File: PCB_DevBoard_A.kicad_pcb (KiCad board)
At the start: 2 copper layers, 83 x 71 mm, 55 parts, among them J1 Conn_01x05, J2 Conn_01x05, J3 Debug, J5 I/O A, J6 I/O B, U1 TLV1117-33, U2 XMC1404_F064, U3 TLE7251, U4 ULN2003A, U5 ULN2003A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

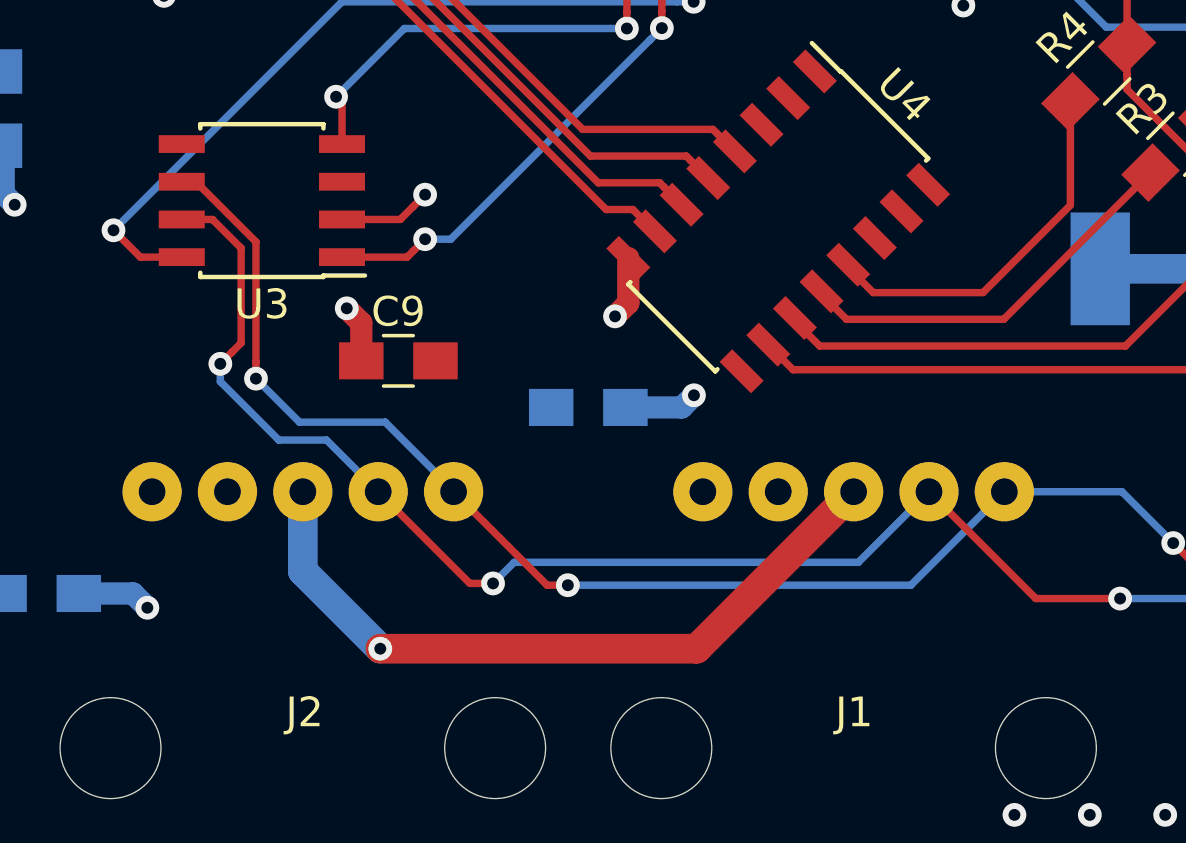
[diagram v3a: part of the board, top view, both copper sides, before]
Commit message: Improve the tracks between the connectors
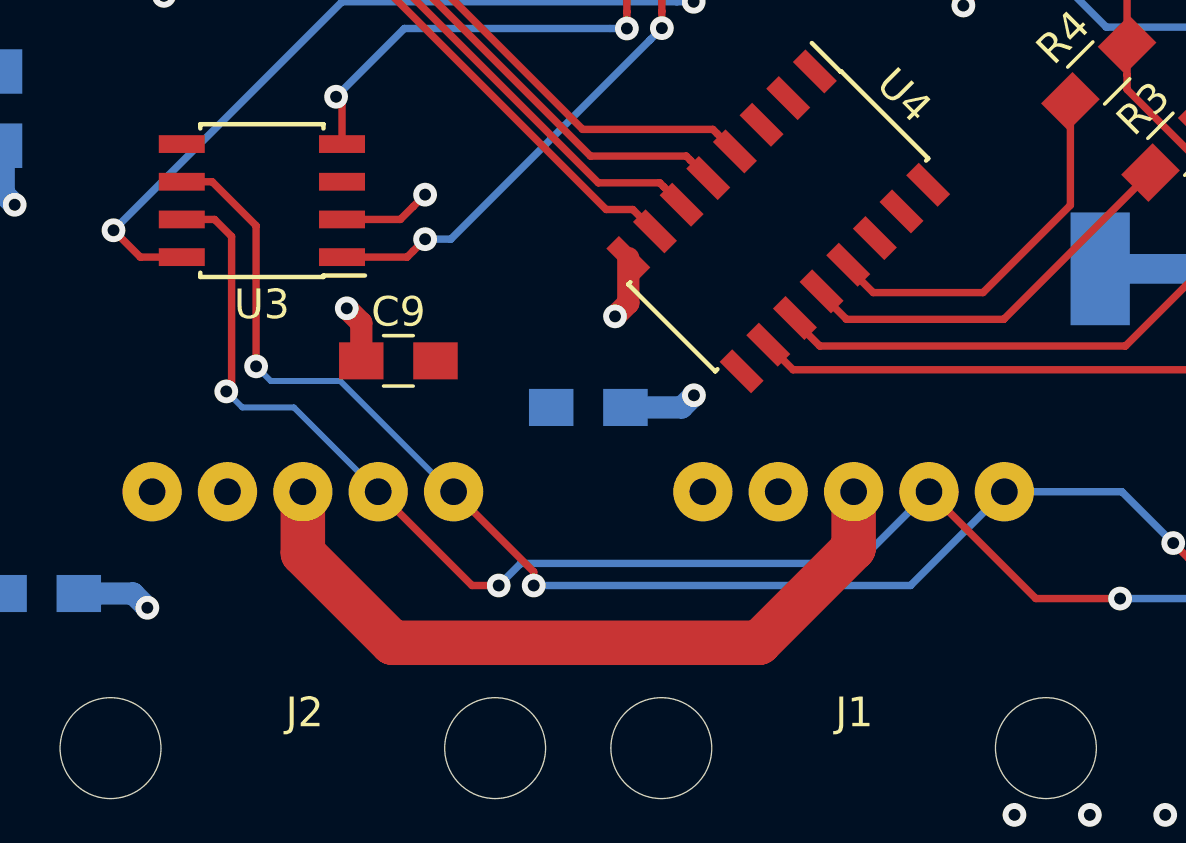
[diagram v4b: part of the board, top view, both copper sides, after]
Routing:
- net +BATT: track 24.5 -> 25.1 mm, vias 1 -> 0
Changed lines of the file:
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@@
     (thickness 1.6)
     (drawings 21)
-    (tracks 711)
+    (tracks 709)
     (zones 0)
     (modules 55)
@@
   )
   (setup
-    (last_trace_width 0.75)
+    (last_trace_width 1.5)
     (user_trace_width 0.75)
     (user_trace_width 1)
+    (user_trace_width 1.5)
     (trace_clearance 0.2)
     (zone_clearance 0.45)
@@
     (via_min_size 0.4)
     (via_min_drill 0.3)
+    (user_via 1.5 0.75)
     (uvia_size 0.3)
     (uvia_drill 0.1)
@@
   (segment (start 121.5 132.15) (end 121.25 132.15) (width 0.25) (layer F.Cu) (net 5))
   (segment (start 121.25 132.15) (end 118.825 134.575) (width 0.25) (layer F.Cu) (net 5))
-  (segment (start 125.3 150.465) (end 125.775 150.465) (width 0.25) (layer F.Cu) (net 6))
-  (segment (start 125.775 150.465) (end 127.80001 152.49001) (width 0.25) (layer F.Cu) (net 6))
-  (segment (start 127.80001 152.49001) (end 127.80001 156.534324) (width 0.25) (layer F.Cu) (net 6))
-  (segment (start 127.80001 156.534324) (end 127.80001 157.100009) (width 0.25) (layer F.Cu) (net 6))
-  (via (at 127.80001 157.100009) (size 0.8) (drill 0.4) (layers F.Cu B.Cu) (net 6))
-  (via (at 138.31 164.06) (size 0.8) (drill 0.4) (layers F.Cu B.Cu) (net 6))
-  (segment (start 134.46 160.91) (end 137.61 164.06) (width 0.25) (layer F.Cu) (net 6))
-  (segment (start 137.61 164.06) (end 138.31 164.06) (width 0.25) (layer F.Cu) (net 6))
-  (segment (start 153.02 160.91) (end 149.87 164.06) (width 0.25) (layer B.Cu) (net 6))
-  (segment (start 149.87 164.06) (end 138.31 164.06) (width 0.25) (layer B.Cu) (net 6))
   (via (at 158.71 162.64) (size 0.8) (drill 0.4) (layers F.Cu B.Cu) (net 6))
   (segment (start 165.37 163.17) (end 159.24 163.17) (width 0.25) (layer F.Cu) (net 6))
@@
   (segment (start 156.98 160.91) (end 158.71 162.64) (width 0.25) (layer B.Cu) (net 6))
   (segment (start 134.46 160.91) (end 134.46 160.87) (width 0.25) (layer B.Cu) (net 6))
-  (segment (start 134.46 160.87) (end 132.154999 158.564999) (width 0.25) (layer B.Cu) (net 6))
-  (segment (start 132.154999 158.564999) (end 129.265001 158.564999) (width 0.25) (layer B.Cu) (net 6))
-  (segment (start 129.265001 158.564999) (end 127.80001 157.100009) (width 0.25) (layer B.Cu) (net 6))
-  (via (at 126.6 156.6) (size 0.8) (drill 0.4) (layers F.Cu B.Cu) (net 7))
-  (segment (start 126.999999 156.200001) (end 126.6 156.6) (width 0.25) (layer F.Cu) (net 7))
-  (segment (start 127.3 155.9) (end 126.999999 156.200001) (width 0.25) (layer F.Cu) (net 7))
-  (segment (start 127.3 152.7) (end 127.3 155.9) (width 0.25) (layer F.Cu) (net 7))
-  (segment (start 125.3 151.735) (end 126.335 151.735) (width 0.25) (layer F.Cu) (net 7))
-  (segment (start 126.335 151.735) (end 127.3 152.7) (width 0.25) (layer F.Cu) (net 7))
-  (via (at 135.79 164.000002) (size 0.8) (drill 0.4) (layers F.Cu B.Cu) (net 7))
-  (segment (start 131.92 160.91) (end 135.010002 164.000002) (width 0.25) (layer F.Cu) (net 7))
-  (segment (start 135.010002 164.000002) (end 135.79 164.000002) (width 0.25) (layer F.Cu) (net 7))
-  (segment (start 150.48 160.91) (end 148.099983 163.290017) (width 0.25) (layer B.Cu) (net 7))
-  (segment (start 148.099983 163.290017) (end 136.499985 163.290017) (width 0.25) (layer B.Cu) (net 7))
-  (segment (start 136.499985 163.290017) (end 135.79 164.000002) (width 0.25) (layer B.Cu) (net 7))
+  (via (at 127.804992 156.685008) (size 0.8) (drill 0.4) (layers F.Cu B.Cu) (net 6))
+  (segment (start 125.3 150.465) (end 126.325 150.465) (width 0.25) (layer F.Cu) (net 6))
+  (segment (start 126.325 150.465) (end 127.804992 151.944992) (width 0.25) (layer F.Cu) (net 6))
+  (segment (start 127.804992 151.944992) (end 127.804992 156.685008) (width 0.25) (layer F.Cu) (net 6))
+  (segment (start 128.299984 157.18) (end 127.804992 156.685008) (width 0.2) (layer B.Cu) (net 6))
+  (segment (start 130.64 157.18) (end 128.299984 157.18) (width 0.2) (layer B.Cu) (net 6))
+  (segment (start 134.37 160.91) (end 130.64 157.18) (width 0.2) (layer B.Cu) (net 6))
+  (segment (start 134.46 160.91) (end 134.37 160.91) (width 0.2) (layer B.Cu) (net 6))
+  (segment (start 153.02 160.91) (end 149.859998 164.070002) (width 0.25) (layer B.Cu) (net 6))
+  (via (at 137.16 164.070002) (size 0.8) (drill 0.4) (layers F.Cu B.Cu) (net 6))
+  (segment (start 149.859998 164.070002) (end 137.16 164.070002) (width 0.25) (layer B.Cu) (net 6))
+  (segment (start 134.46 160.91) (end 137.16 163.61) (width 0.25) (layer F.Cu) (net 6))
+  (segment (start 137.16 163.61) (end 137.16 164.070002) (width 0.25) (layer F.Cu) (net 6))
   (via (at 156.92 164.51) (size 0.8) (drill 0.4) (layers F.Cu B.Cu) (net 7))
   (segment (start 150.48 160.91) (end 154.08 164.51) (width 0.25) (layer F.Cu) (net 7))
@@
   (segment (start 165.56 167.47) (end 162.6 164.51) (width 0.25) (layer B.Cu) (net 7))
   (segment (start 162.6 164.51) (end 156.92 164.51) (width 0.25) (layer B.Cu) (net 7))
-  (segment (start 126.6 156.6) (end 126.6 157.2) (width 0.25) (layer B.Cu) (net 7))
-  (segment (start 126.6 157.2) (end 128.57 159.17) (width 0.25) (layer B.Cu) (net 7))
-  (segment (start 128.57 159.17) (end 130.18 159.17) (width 0.25) (layer B.Cu) (net 7))
-  (segment (start 130.18 159.17) (end 131.92 160.91) (width 0.25) (layer B.Cu) (net 7))
+  (via (at 126.8 157.53) (size 0.8) (drill 0.4) (layers F.Cu B.Cu) (net 7))
+  (segment (start 127.34 158.07) (end 126.8 157.53) (width 0.2) (layer B.Cu) (net 7))
+  (segment (start 129.08 158.07) (end 127.34 158.07) (width 0.2) (layer B.Cu) (net 7))
+  (segment (start 131.92 160.91) (end 129.08 158.07) (width 0.2) (layer B.Cu) (net 7))
+  (segment (start 126.98 157.35) (end 126.8 157.53) (width 0.25) (layer F.Cu) (net 7))
+  (segment (start 126.98 152.31) (end 126.98 157.35) (width 0.25) (layer F.Cu) (net 7))
+  (segment (start 126.405 151.735) (end 126.98 152.31) (width 0.25) (layer F.Cu) (net 7))
+  (segment (start 125.3 151.735) (end 126.405 151.735) (width 0.25) (layer F.Cu) (net 7))
+  (via (at 135.980002 164.07) (size 0.8) (drill 0.4) (layers F.Cu B.Cu) (net 7))
+  (segment (start 131.92 160.91) (end 135.08 164.07) (width 0.25) (layer F.Cu) (net 7))
+  (segment (start 135.08 164.07) (end 135.980002 164.07) (width 0.25) (layer F.Cu) (net 7))
+  (segment (start 136.725004 163.324998) (end 135.980002 164.07) (width 0.25) (layer B.Cu) (net 7))
+  (segment (start 148.065002 163.324998) (end 136.725004 163.324998) (width 0.25) (layer B.Cu) (net 7))
+  (segment (start 150.48 160.91) (end 148.065002 163.324998) (width 0.25) (layer B.Cu) (net 7))
   (segment (start 126.41 109.875) (end 126.41 111.95) (width 0.25) (layer F.Cu) (net 8))
   (segment (start 133.7 119.24) (end 133.7 120.134315) (width 0.25) (layer F.Cu) (net 8))
@@
   (segment (start 129.749967 138.989373) (end 130.484568 138.254772) (width 0.25) (layer F.Cu) (net 80))
   (segment (start 140.5 151.4) (end 139.6 151.4) (width 0.25) (layer F.Cu) (net 80))
-  (via (at 131.99 166.2) (size 0.8) (drill 0.4) (layers F.Cu B.Cu) (net 104))
-  (segment (start 142.65 166.2) (end 131.99 166.2) (width 1) (layer F.Cu) (net 104))
-  (segment (start 147.94 160.91) (end 142.65 166.2) (width 1) (layer F.Cu) (net 104))
-  (segment (start 129.38 163.59) (end 131.99 166.2) (width 1) (layer B.Cu) (net 104))
-  (segment (start 129.38 160.91) (end 129.38 163.59) (width 1) (layer B.Cu) (net 104))
+  (segment (start 147.94 162.81) (end 147.94 160.91) (width 1.5) (layer F.Cu) (net 104))
+  (segment (start 132.4 166) (end 144.75 166) (width 1.5) (layer F.Cu) (net 104))
+  (segment (start 129.38 162.98) (end 132.4 166) (width 1.5) (layer F.Cu) (net 104))
+  (segment (start 144.75 166) (end 147.94 162.81) (width 1.5) (layer F.Cu) (net 104))
+  (segment (start 129.38 160.91) (end 129.38 162.98) (width 1.5) (layer F.Cu) (net 104))
   (segment (start 168.07 167.44) (end 168.1 167.47) (width 0.25) (layer F.Cu) (net 105))
   (segment (start 168.07 163.17) (end 168.07 167.44) (width 0.25) (layer F.Cu) (net 105))

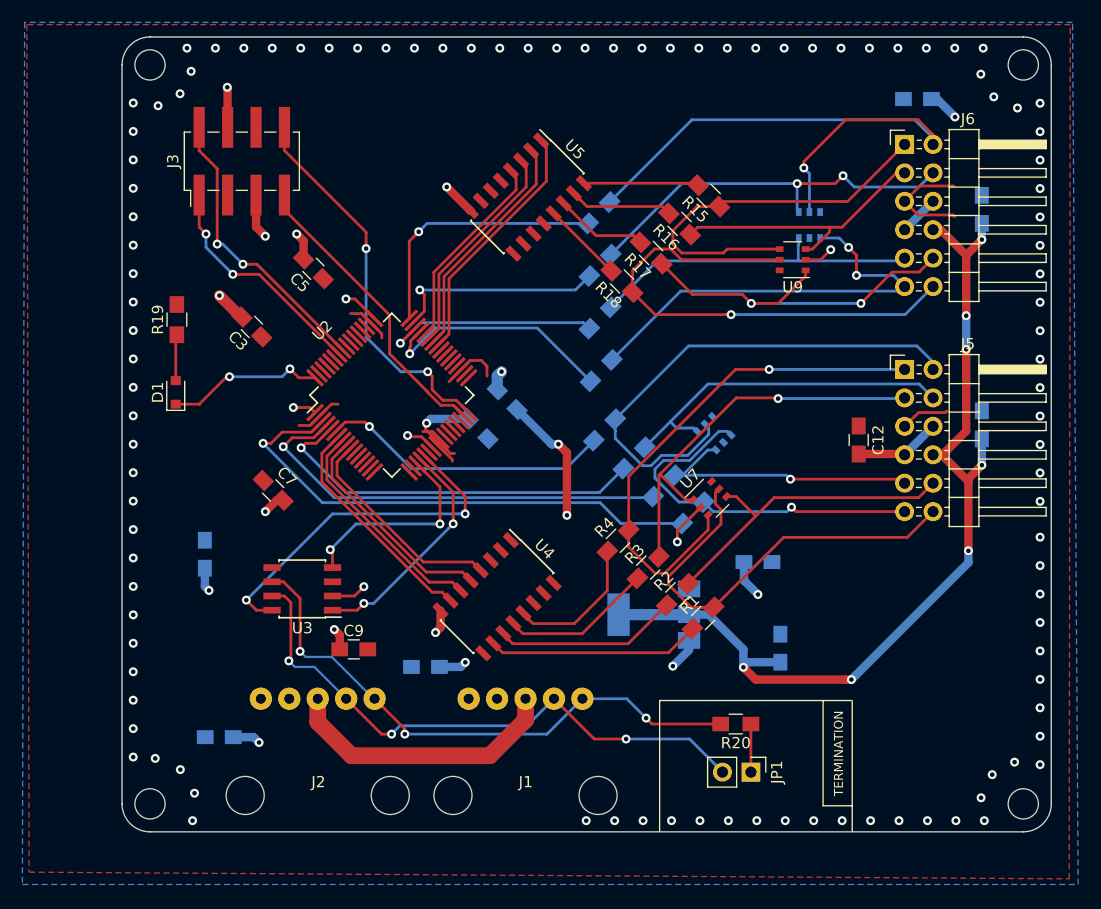
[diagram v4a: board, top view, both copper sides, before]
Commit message: Remove the ground vias around the edges
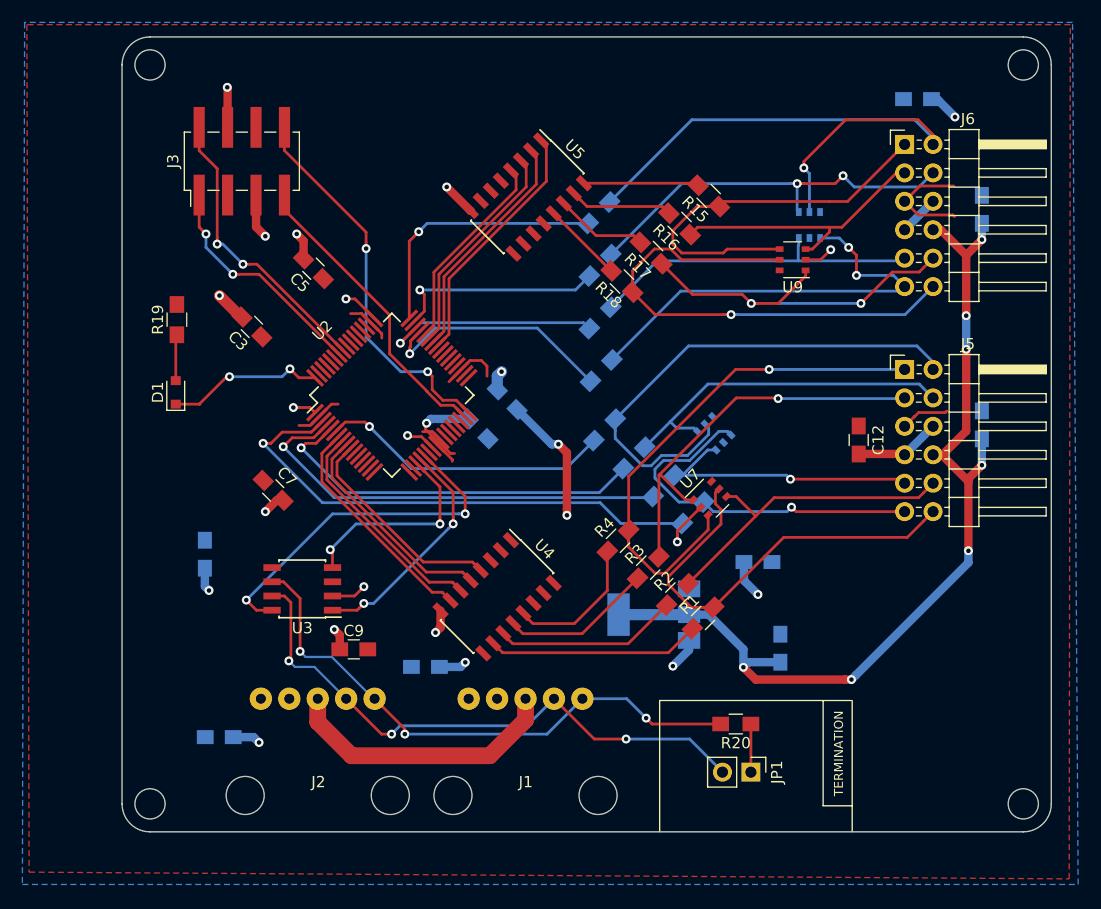
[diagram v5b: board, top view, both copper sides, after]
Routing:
- net GND: vias 121 -> 16

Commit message: Update logotypes etc.
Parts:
- removed the G*** at (129.9, 112.0)
- added G***: LOGO, DevBoard:Text_Wolley_DevECU_14mm_SilkScreen, B.Cu at (121.2, 126.5)
- G***: moved to F.Cu
- moved G*** 60.8 mm to (184.2, 157.2), turned to 0 degrees
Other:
- board text added: "BUS"
- board text removed: "DevBoard A 1.0"

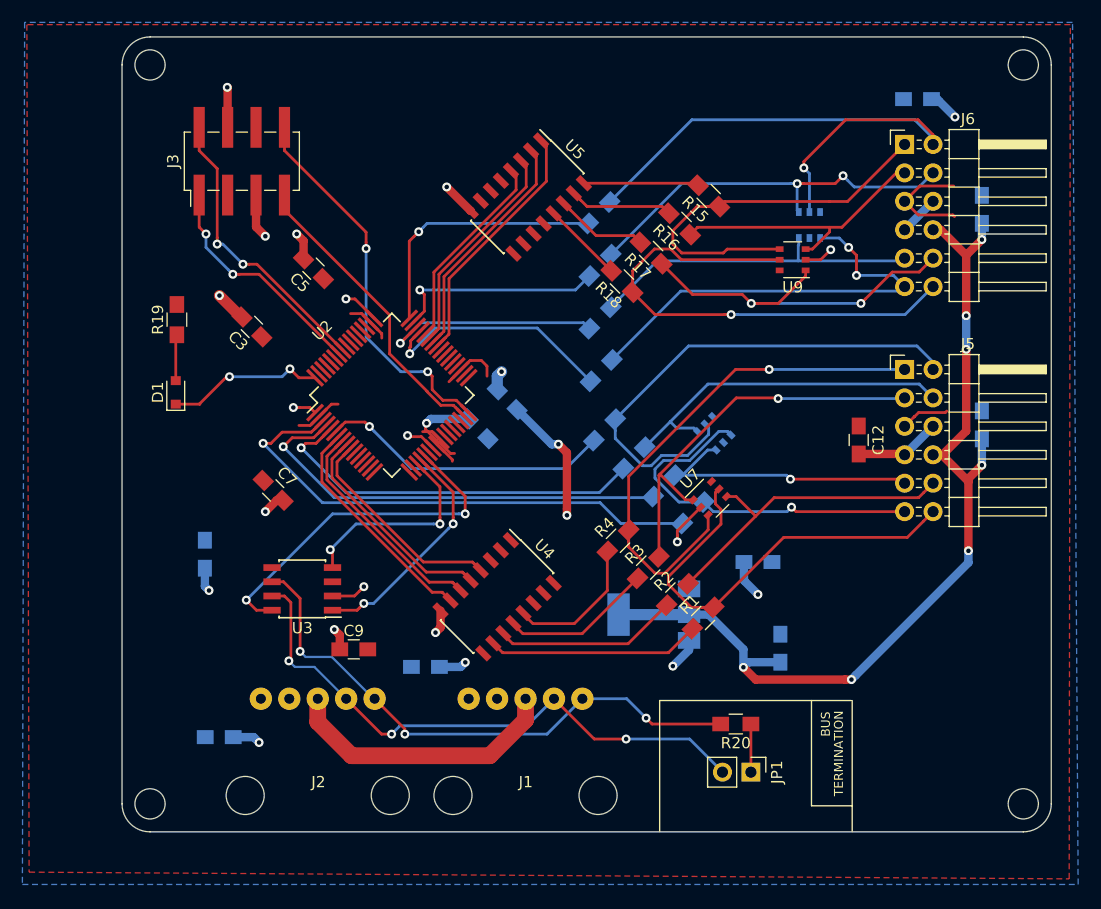
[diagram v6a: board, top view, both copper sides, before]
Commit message: Replace the M2.5 mounting holes with M3 holes
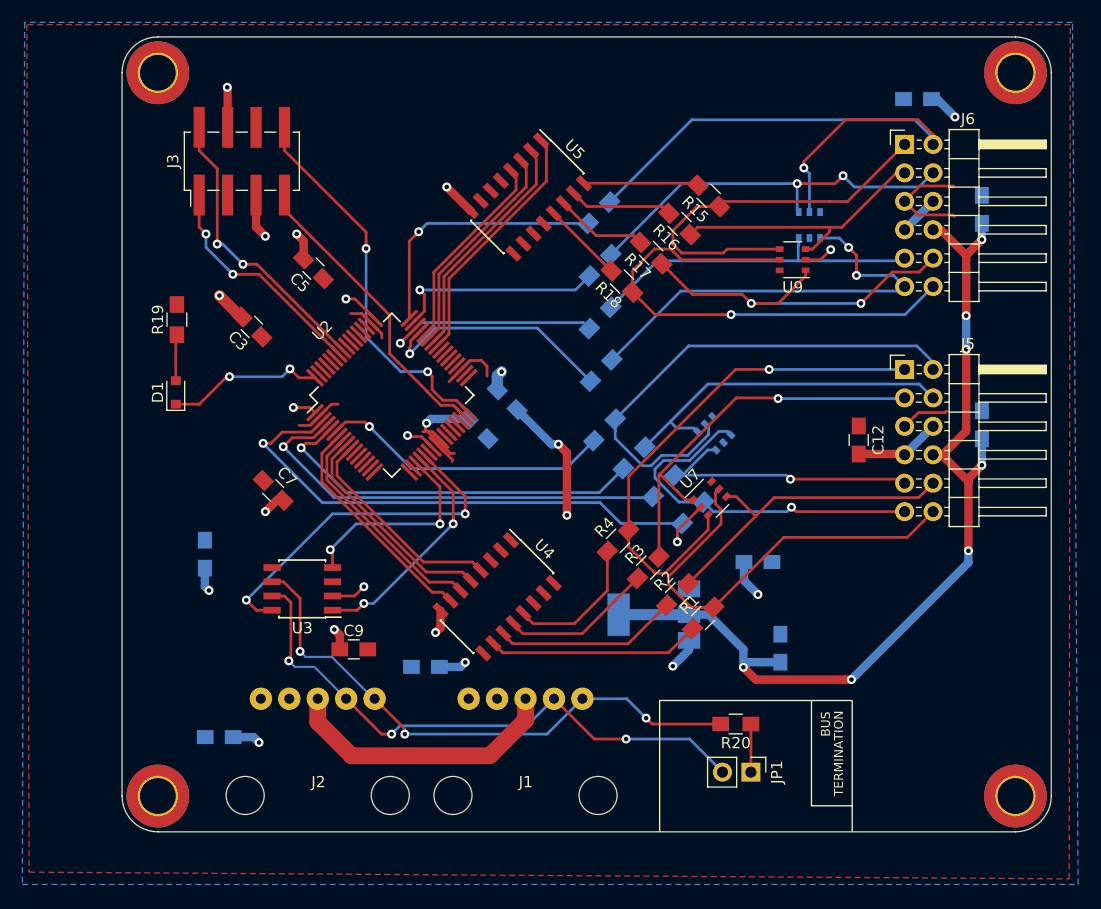
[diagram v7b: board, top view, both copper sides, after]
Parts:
- removed the REF** at (192.4, 104.3)
- removed the REF** at (114.4, 104.3)
- removed the REF** at (114.4, 170.3)
- removed the REF** at (192.4, 170.3)
- added REF**: MountingHole_3.2mm_M3_DIN965_Pad_TopBottom, MountingHole:MountingHole_3.2mm_M3_DIN965_Pad_TopBottom, F.Cu at (191.7, 169.6)
- added REF**: MountingHole_3.2mm_M3_DIN965_Pad_TopBottom, MountingHole:MountingHole_3.2mm_M3_DIN965_Pad_TopBottom, F.Cu at (115.1, 169.6)
- added REF**: MountingHole_3.2mm_M3_DIN965_Pad_TopBottom, MountingHole:MountingHole_3.2mm_M3_DIN965_Pad_TopBottom, F.Cu at (115.1, 105.0)
- added REF**: MountingHole_3.2mm_M3_DIN965_Pad_TopBottom, MountingHole:MountingHole_3.2mm_M3_DIN965_Pad_TopBottom, F.Cu at (191.7, 105.0)
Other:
- outline, holes or cut-outs redrawn
